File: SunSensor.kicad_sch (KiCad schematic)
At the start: 6 parts, among them U1 AD7291BCPZ

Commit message: Finished schematic and finalized parts
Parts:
- removed D1, D2, D3, D4, D5: K857PH, K857PH, symbol Diode:K857PH
- added AlertLED: (no value), Display:HDSP-4836, symbol LED:HDSP-4836
- added C?: 1 µF, symbol Device:C
- added C?: 100 µF, symbol Device:C
- added C?: 100 nF, symbol Device:C
- added L? (x5): Adafruit_VEML7700_Lux_Sensor, symbol Sensor_Optical:Adafruit_VEML7700_Lux_Sensor
- added R? (x5): NSL-7910, symbol Device:R_Photo
- added R? (x5): 50k_Ohms, symbol Device:50k_Ohms
- added R?: 1k_ohms, symbol Device:50k_Ohms
- added U?: TCA9548A_Multiplexer, symbol Analog_Switch:TCA9548A_Multiplexer
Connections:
- net GNDREF: now also L?.3 (GND), L?.3 (GND), L?.3 (GND), L?.3 (GND), L?.3 (GND), R?.2, R?.2, R?.2, R?.2, R?.2, R?.2
- net GNDS: now also U1.18 (VIN0), U1.4 (VIN6), U1.5 (VIN7), C?.2, C?.2, C?.2
- net Vin3: now reaches U1.1 (VIN3)
- net Vin3: now also R?.1, R?.2
- net +3V3: now reaches U1.10 (VDD)
- net +3V3: now also C?.1, C?.1
- net at U1.12 (Alert): now also AlertLED.1 (A)
- net Vin1: now reaches U1.19 (VIN1)
- net Vin1: now also R?.1, R?.2
- net Vin4: now reaches U1.2 (VIN4)
- net Vin4: now also R?.1, R?.2
- net Vin2: now reaches U1.20 (VIN2)
- net Vin2: now also R?.1, R?.2
- net Vin5: now reaches U1.3 (VIN5)
- net Vin5: now also R?.1, R?.2
- net V_ref: now reaches U1.7 (VREF)
- net V_ref: now also R?.1, R?.1, R?.1, R?.1, R?.1
- net at U1.8 (DCAP): now also C?.1
- new net: L?.4 (SCL), U?.5 (SCL0)
- new net: L?.5 (SDA), U?.4 (SDA0)
- new net: L?.4 (SCL), U?.11 (SCL3)
- new net: L?.5 (SDA), U?.10 (SDA3)
- new net: L?.4 (SCL), U?.14 (SCL4)
- new net: L?.5 (SDA), U?.13 (SDA4)
- new net: L?.4 (SCL), U?.7 (SCL1)
- new net: L?.5 (SDA), U?.6 (SDA1)
- new net: L?.4 (SCL), U?.9 (SCL2)
- new net: L?.5 (SDA), U?.8 (SDA2)
- new net: AlertLED.20 (K), R?.1
- new net +5V: L?.1 (Vin), L?.1 (Vin), L?.1 (Vin), L?.1 (Vin), L?.1 (Vin)
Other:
- moved on the sheet: U1

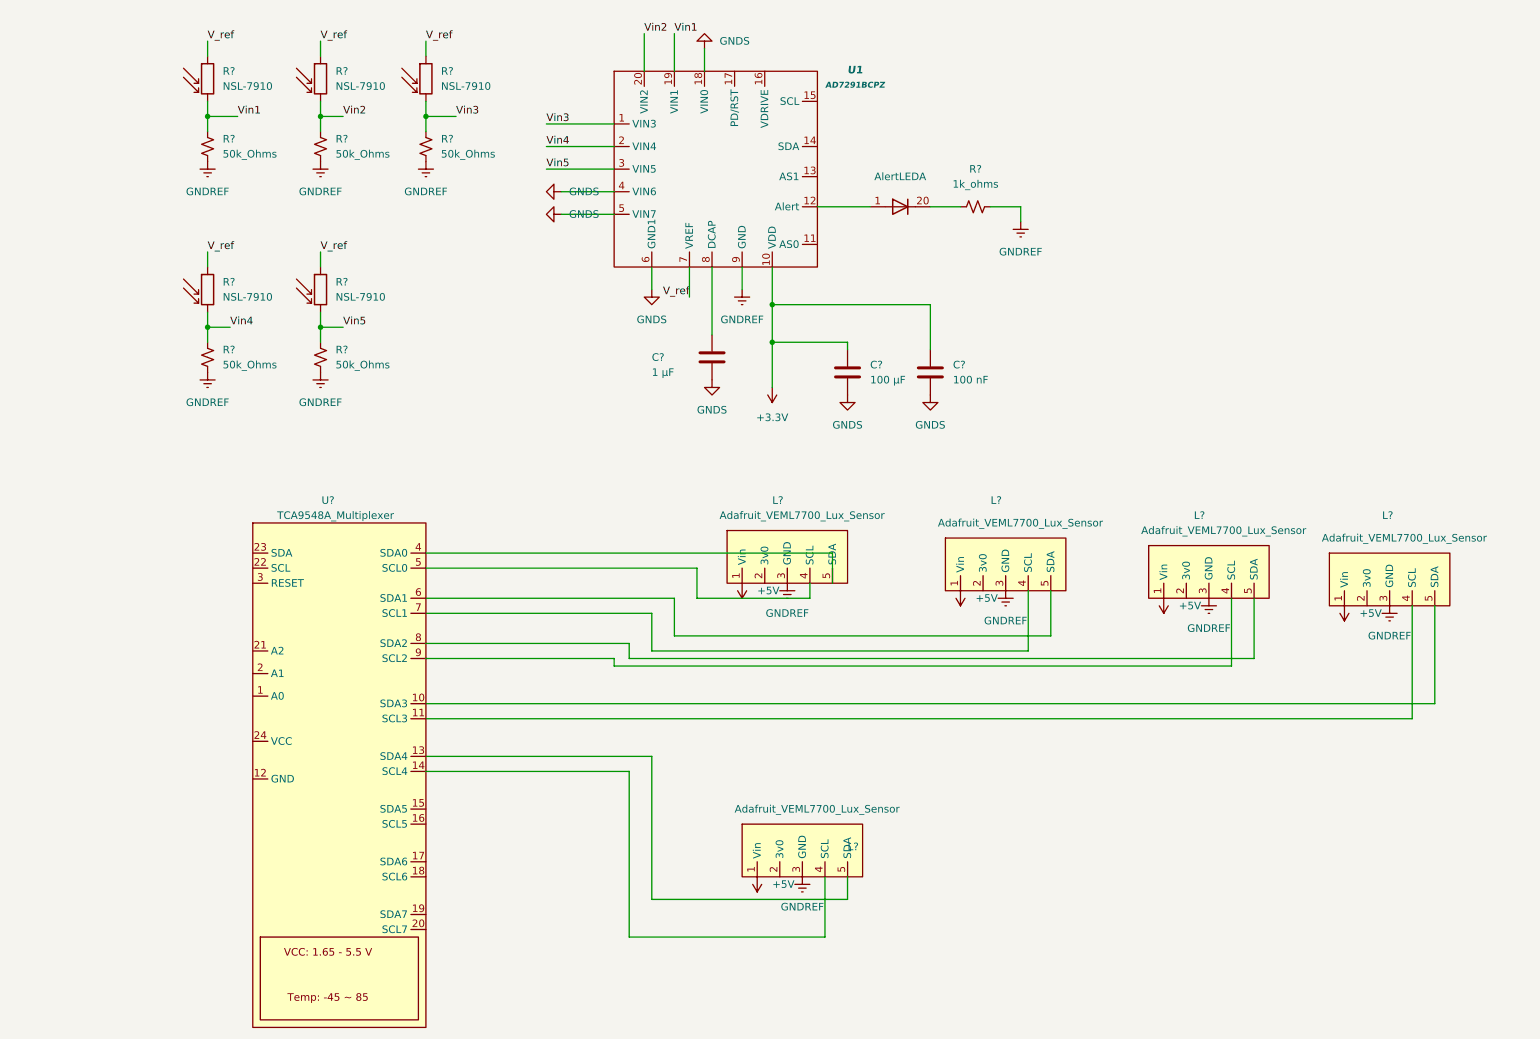
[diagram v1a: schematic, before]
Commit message: Added footprints and library to Sunsensor
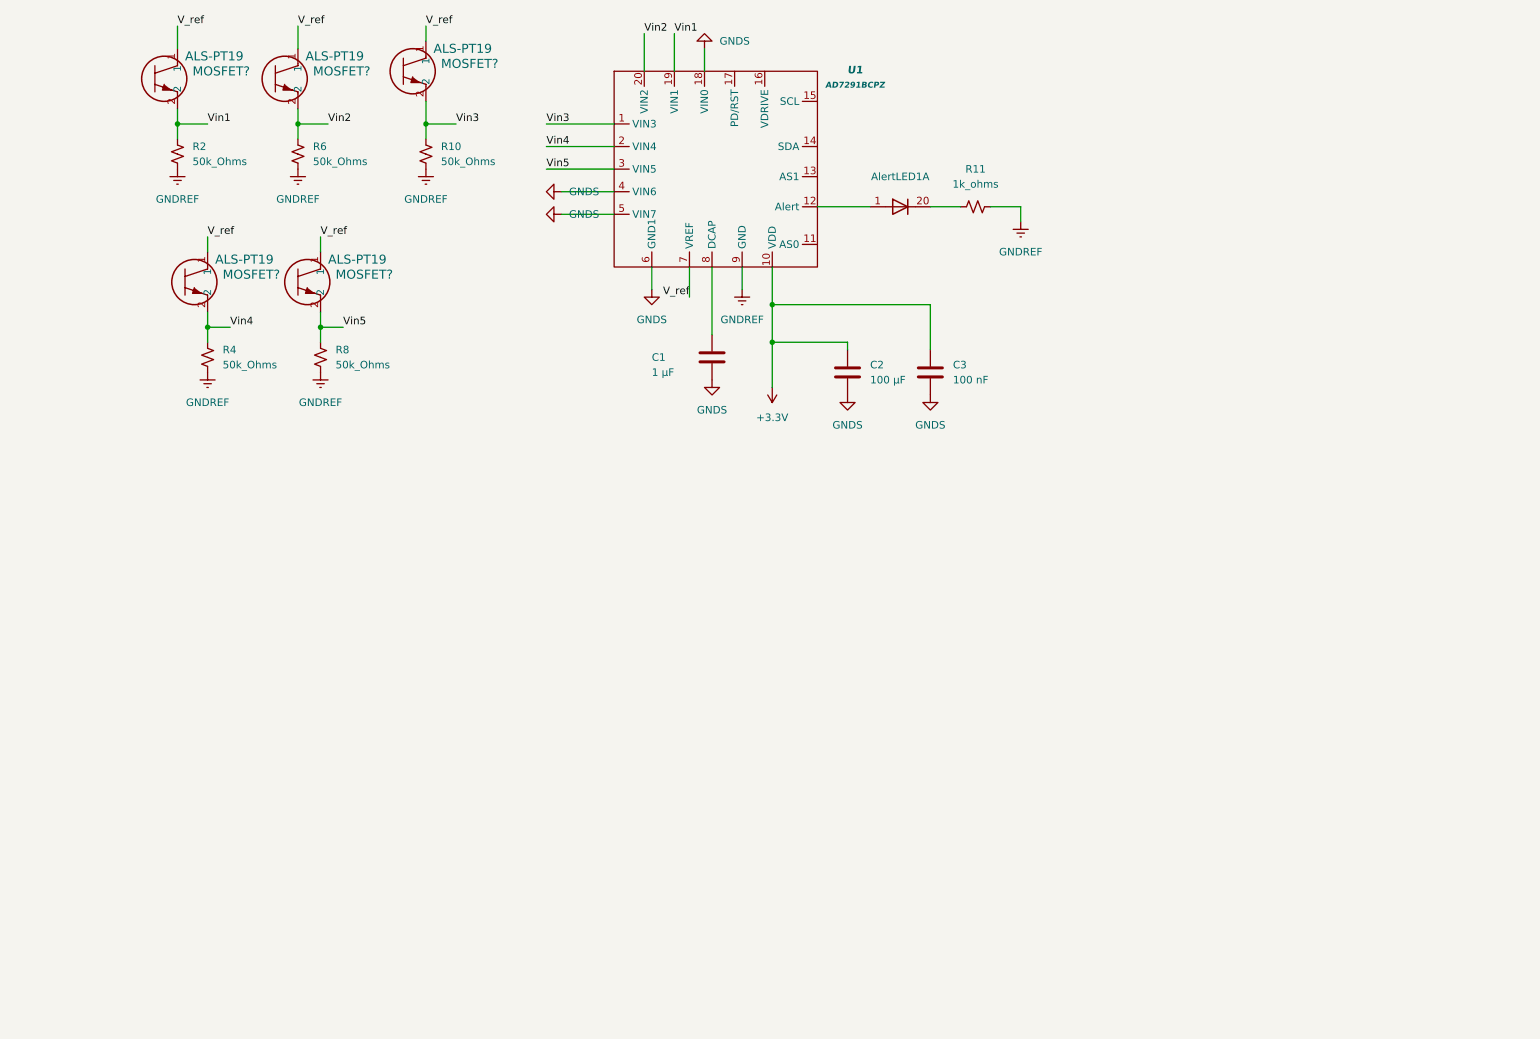
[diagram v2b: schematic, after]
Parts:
- removed L? (x5): Adafruit_VEML7700_Lux_Sensor, symbol Sensor_Optical:Adafruit_VEML7700_Lux_Sensor
- removed R? (x5): NSL-7910, symbol Device:R_Photo
- removed U?: TCA9548A_Multiplexer, symbol Analog_Switch:TCA9548A_Multiplexer
- added MOSFET? (x5): ALS-PT19, sunsensor:LED_77&slash_TR8_EVE, symbol 4xxx:ALS-PT19-315C_L177_TR8
- gave numbers to parts that had none: 9
- renumbered AlertLED to AlertLED1
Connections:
- net V_ref: now also MOSFET?.1, MOSFET?.1, MOSFET?.1, MOSFET?.1, MOSFET?.1
- net Vin1: now also MOSFET?.2
- net Vin2: now also MOSFET?.2
- net Vin3: now also MOSFET?.2
- net Vin4: now also MOSFET?.2
- net Vin5: now also MOSFET?.2
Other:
- moved on the sheet: R10, R2, R6
